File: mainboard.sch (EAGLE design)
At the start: 1 part

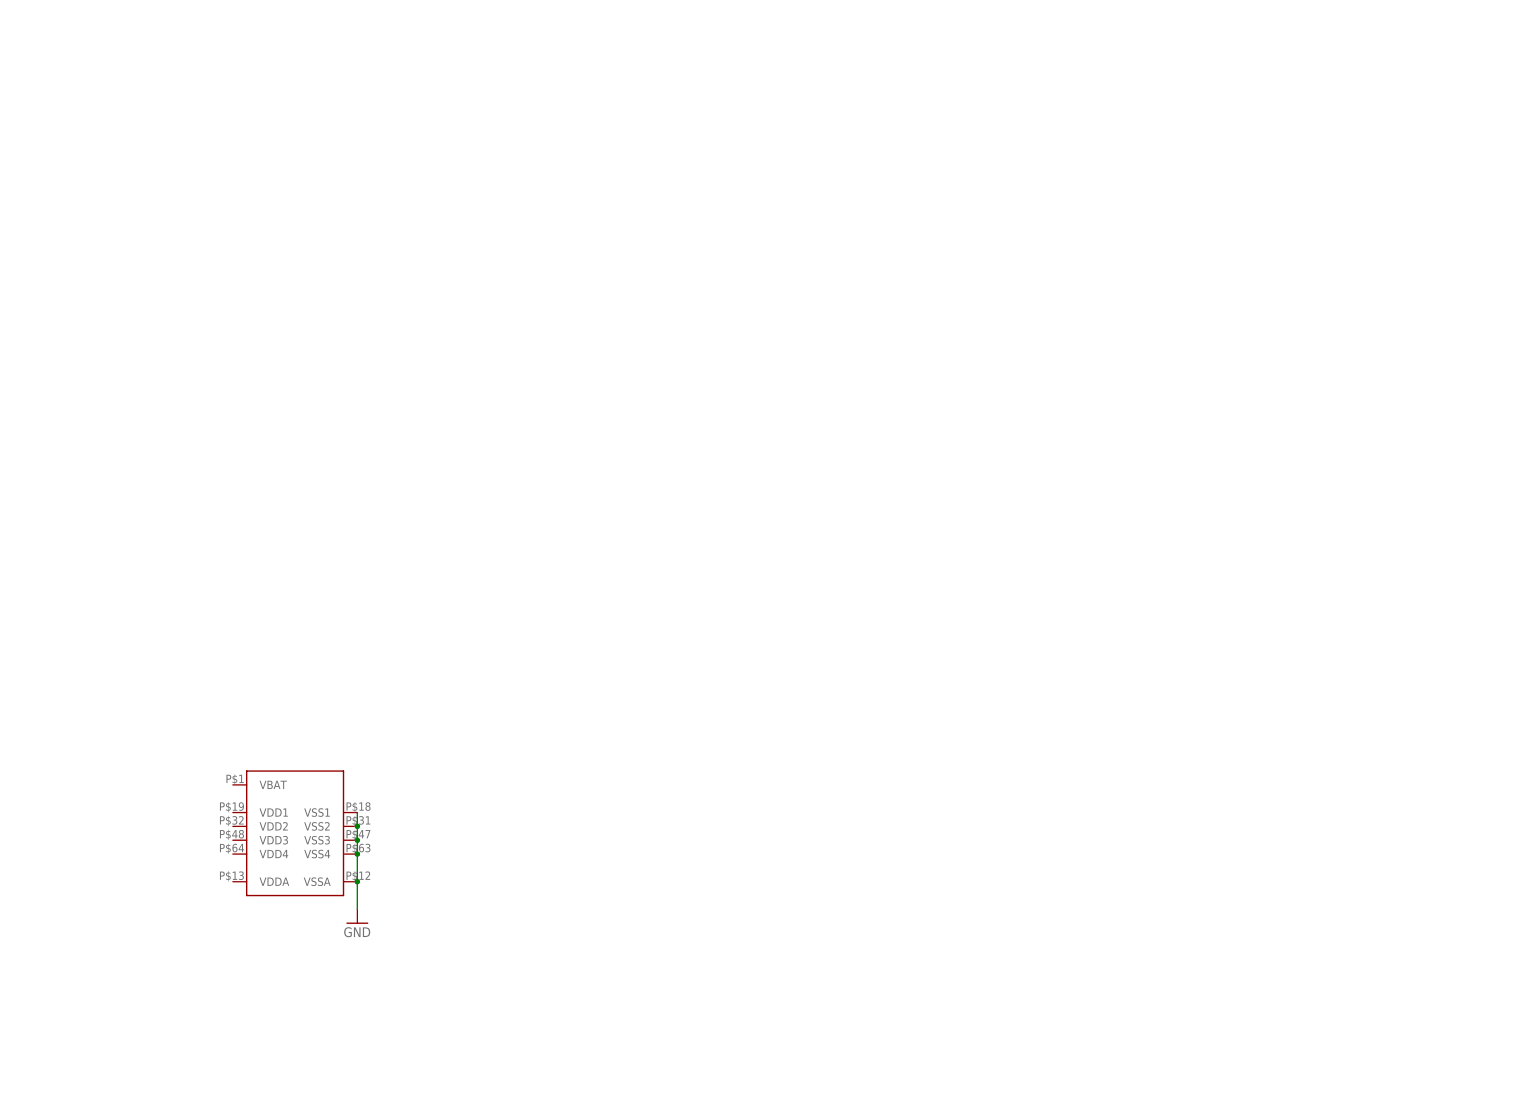
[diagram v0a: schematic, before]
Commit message: Features added in schematic
Power supplies (+3.3 and 12v)
Button matrix
Microprocessor and support circuitry
Programming headers
SD Card reader
OLED Screen connector
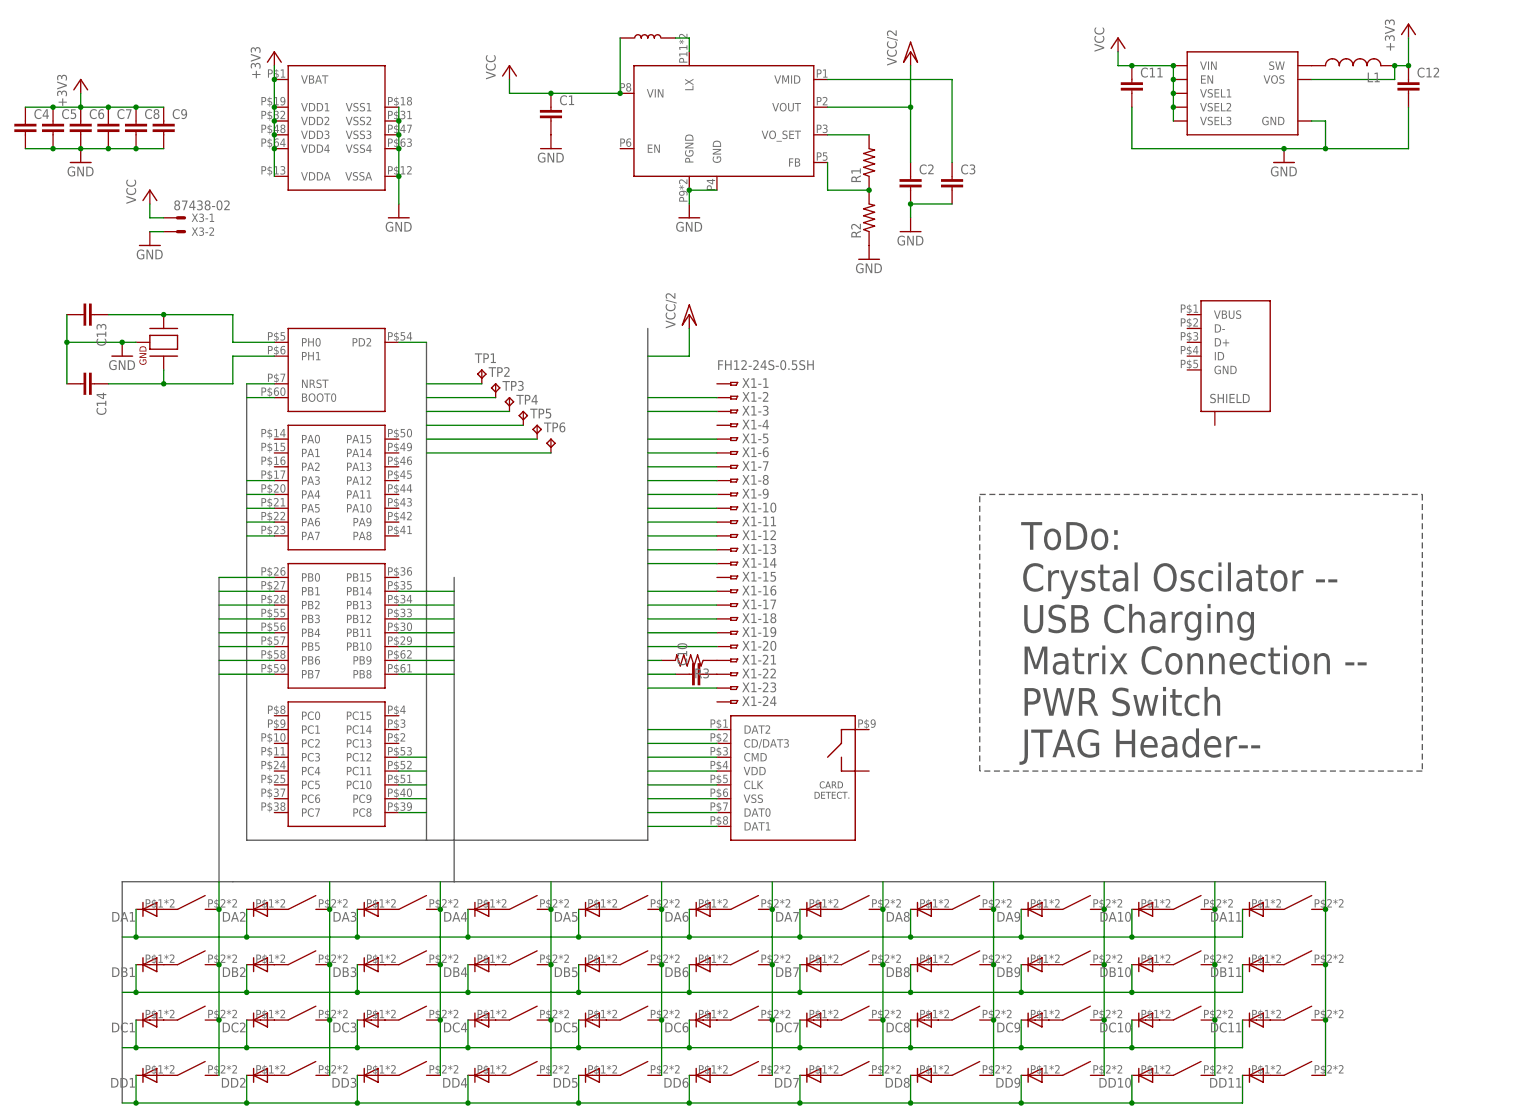
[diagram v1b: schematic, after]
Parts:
- added BTA1, BTA10, BTA11, BTA2, BTA3, BTA4, BTA5, BTA6, BTA7, BTA8, BTA9, BTB1, BTB10, BTB11, BTB2, BTB3, BTB4, BTB5, BTB6, BTB7, BTB8, BTB9, BTC1, BTC10, BTC11, BTC2, BTC3, BTC4, BTC5, BTC6, BTC7, BTC8, BTC9, BTD1, BTD10, BTD11, BTD2, BTD3, BTD4, BTD5, BTD6, BTD7, BTD8, BTD9: WURTH_SWITCH, lib:WURTH_SWITCH
- added C1, C2, C3: (no value), resistor:C-EUC0805
- added C10, C11, C12, C4, C5, C6, C7, C8, C9: (no value), rcl:C-EUC0603
- added C13, C14: (no value), eagle-ltspice:CC0603
- added DA1, DA10, DA11, DA2, DA3, DA4, DA5, DA6, DA7, DA8, DA9, DB1, DB10, DB11, DB2, DB3, DB4, DB5, DB6, DB7, DB8, DB9, DC1, DC10, DC11, DC2, DC3, DC4, DC5, DC6, DC7, DC8, DC9, DD1, DD10, DD11, DD2, DD3, DD4, DD5, DD6, DD7, DD8, DD9: (no value), diode:DIODE-SOD523
- added L1: (no value), rcl:L-USL2012C
- added R1, R2, R3: (no value), resistor:R-US_R0402
- added TP1, TP2, TP3, TP4, TP5, TP6: TPTP20SQ, testpad:TPTP20SQ
- added U$2: DM3AT-SF-PEJM5, lib:DM3AT-SF-PEJM5
- added U$3: MOLEX_47346-1001, lib:MOLEX_47346-1001
- added U$4: STOD1317BTPUR, lib:STOD1317BTPUR
- added U$5: VLS252010HBU, lib:VLS252010HBU
- added U$6: TPS627431YFPR, lib:TPS627431YFPR
- added U$7: CX5032SA, lib:CX5032SA
- added X1: FH12-24S-0.5SH, con-hirose:FH12-24S-0.5SH
- added X3: 87438-02, con-molex:87438-02
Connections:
- new net +3V3: C12.1, C4.1, C5.1, C6.1, C7.1, C8.1, C9.1, L1.2, TP1.TP, U$1G$1.VBAT, U$1G$1.VDD1, U$1G$1.VDD2, U$1G$1.VDD3, U$1G$1.VDD4, U$1G$1.VDDA, U$2.VDD, U$6.VOS, X1-5.1, X1-9.1
- new net BOOT0: TP5.TP, U$1G$5.BOOT0
- new net KEYCOL0: BTA1.P$2, BTB1.P$2, BTC1.P$2, BTD1.P$2, U$1G$3.PB0
- new net KEYCOL1: BTA2.P$2, BTB2.P$2, BTC2.P$2, BTD2.P$2, U$1G$3.PB1
- new net KEYCOL10: BTA11.P$2, BTB11.P$2, BTC11.P$2, BTD11.P$2, U$1G$3.PB10
- new net KEYCOL2: BTA3.P$2, BTB3.P$2, BTC3.P$2, BTD3.P$2, U$1G$3.PB2
- new net KEYCOL3: BTA4.P$2, BTB4.P$2, BTC4.P$2, BTD4.P$2, U$1G$3.PB3
- new net KEYCOL4: BTA5.P$2, BTB5.P$2, BTC5.P$2, BTD5.P$2, U$1G$3.PB4
- new net KEYCOL5: BTA6.P$2, BTB6.P$2, BTC6.P$2, BTD6.P$2, U$1G$3.PB5
- new net KEYCOL6: BTA7.P$2, BTB7.P$2, BTC7.P$2, BTD7.P$2, U$1G$3.PB6
- new net KEYCOL7: BTA8.P$2, BTB8.P$2, BTC8.P$2, BTD8.P$2, U$1G$3.PB7
- new net KEYCOL8: BTA9.P$2, BTB9.P$2, BTC9.P$2, BTD9.P$2, U$1G$3.PB8
- new net KEYCOL9: BTA10.P$2, BTB10.P$2, BTC10.P$2, BTD10.P$2, U$1G$3.PB9
- new net KEYROW0: DA1.C, DA10.C, DA11.C, DA2.C, DA3.C, DA4.C, DA5.C, DA6.C, DA7.C, DA8.C, DA9.C
- new net KEYROW1: DB1.C, DB10.C, DB11.C, DB2.C, DB3.C, DB4.C, DB5.C, DB6.C, DB7.C, DB8.C, DB9.C, U$1G$3.PB13
- new net KEYROW2: DC1.C, DC10.C, DC11.C, DC2.C, DC3.C, DC4.C, DC5.C, DC6.C, DC7.C, DC8.C, DC9.C, U$1G$3.PB12
- new net KEYROW3: DD1.C, DD10.C, DD11.C, DD2.C, DD3.C, DD4.C, DD5.C, DD6.C, DD7.C, DD8.C, DD9.C, U$1G$3.PB11, U$1G$3.PB14
- new net N$1: U$4.LX, U$5.P$2
- new net N$10: BTA3.P$1, DA3.A
- new net N$11: BTA4.P$1, DA4.A
- new net N$12: BTA5.P$1, DA5.A
- new net N$13: BTA6.P$1, DA6.A
- new net N$14: BTA7.P$1, DA7.A
- new net N$15: BTA8.P$1, DA8.A
- new net N$16: BTA9.P$1, DA9.A
- new net N$17: BTA10.P$1, DA10.A
- new net N$18: BTA11.P$1, DA11.A
- new net N$19: BTB1.P$1, DB1.A
- new net N$2: R1.1, R2.2, U$4.FB
- new net N$20: BTB2.P$1, DB2.A
- new net N$21: BTB3.P$1, DB3.A
- new net N$22: BTB4.P$1, DB4.A
- new net N$23: BTB5.P$1, DB5.A
- new net N$24: BTB6.P$1, DB6.A
- new net N$25: BTB7.P$1, DB7.A
- new net N$26: BTB8.P$1, DB8.A
- new net N$27: BTB9.P$1, DB9.A
- new net N$28: BTB10.P$1, DB10.A
- new net N$29: BTB11.P$1, DB11.A
- new net N$3: R3.1, X1-21.1
- new net N$30: BTC1.P$1, DC1.A
- new net N$31: BTC2.P$1, DC2.A
- new net N$32: BTC3.P$1, DC3.A
- new net N$33: BTC4.P$1, DC4.A
- new net N$34: BTC5.P$1, DC5.A
- new net N$35: BTC6.P$1, DC6.A
- new net N$36: BTC7.P$1, DC7.A
- new net N$37: BTC8.P$1, DC8.A
- new net N$38: BTC9.P$1, DC9.A
- new net N$39: BTC10.P$1, DC10.A
- new net N$4: R1.2, U$4.VO_SET
- new net N$40: BTC11.P$1, DC11.A
- new net N$41: BTD1.P$1, DD1.A
- new net N$42: BTD2.P$1, DD2.A
- new net N$43: BTD3.P$1, DD3.A
- new net N$44: BTD4.P$1, DD4.A
- new net N$45: BTD5.P$1, DD5.A
- new net N$46: BTD6.P$1, DD6.A
- new net N$47: BTD7.P$1, DD7.A
- new net N$48: BTD8.P$1, DD8.A
- new net N$49: BTD9.P$1, DD9.A
- new net N$5: C10.2, X1-22.1
- new net N$50: BTD10.P$1, DD10.A
- new net N$51: BTD11.P$1, DD11.A
- new net N$52: C13.1, U$1G$5.PH0, U$7.P1
- new net N$53: C14.1, U$1G$5.PH1, U$7.P2
- new net N$6: C3.1, U$4.VMID
- new net N$7: L1.1, U$6.SW
- new net N$8: BTA1.P$1, DA1.A
- new net N$9: BTA2.P$1, DA2.A
- new net NRST: TP6.TP, U$1G$5.NRST
- new net PA13: TP2.TP
- new net PA14: TP3.TP
- new net PA3: U$1G$2.PA3, X1-10.1
- new net SD_CLK: U$1G$4.PC12, U$2.CLK
- new net SD_CMD: U$1G$5.PD2, U$2.CMD
- new net SD_DAT0: U$1G$4.PC8, U$2.DAT0
- new net SD_DAT1: U$1G$4.PC9, U$2.DAT1
- new net SD_DAT2: U$1G$4.PC10, U$2.DAT2
- new net SD_DAT3: U$1G$4.PC11, U$2.CD/DAT3
- new net SPI_CS: U$1G$2.PA4, X1-8.1
- new net SPI_MISO: U$1G$2.PA6
- new net SPI_MOSI: U$1G$2.PA7, X1-14.1
- new net SPI_SCK: U$1G$2.PA5, X1-13.1
- new net VCC: C1.1, C11.1, U$4.VIN, U$5.P$1, U$6.EN, U$6.VIN, U$6.VSEL1, U$6.VSEL2, U$6.VSEL3, X3-1.S
- new net VCC/2: C2.1, U$4.VOUT, X1-23.1
- net GND: now also C1.2, C10.1, C11.2, C12.2, C13.2, C14.2, C2.2, C3.2, C4.2, C5.2, C6.2, C7.2, C8.2, C9.2, R2.1, R3.2, TP4.TP, U$2.VSS, U$4.GND, U$4.PGND, U$6.GND, U$7.GND, X1-11.1, X1-12.1, X1-16.1, X1-17.1, X1-18.1, X1-19.1, X1-2.1, X1-20.1, X1-3.1, X1-6.1, X1-7.1, X3-2.S
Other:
- note added: "ToDo: Crystal Oscilator -- USB Charging Matrix Connection -- PWR Switch JTAG Header--"
